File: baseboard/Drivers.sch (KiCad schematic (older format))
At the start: 9 parts, among them J6 Conn_01x08_Male, J7 Conn_01x08_Male, J8 CONN_01x06, J9 CONN_01x06

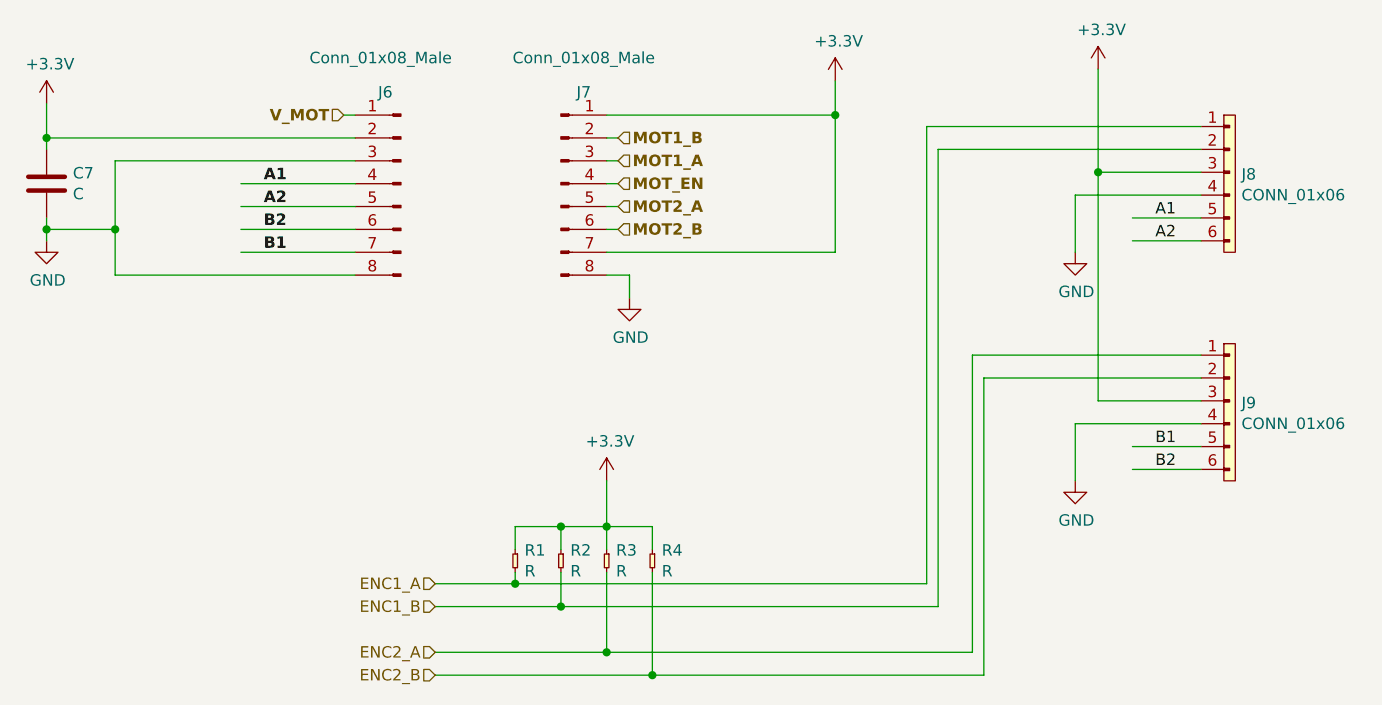
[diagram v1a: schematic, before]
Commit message: standalone version of unav2 based on stm32f405rgt
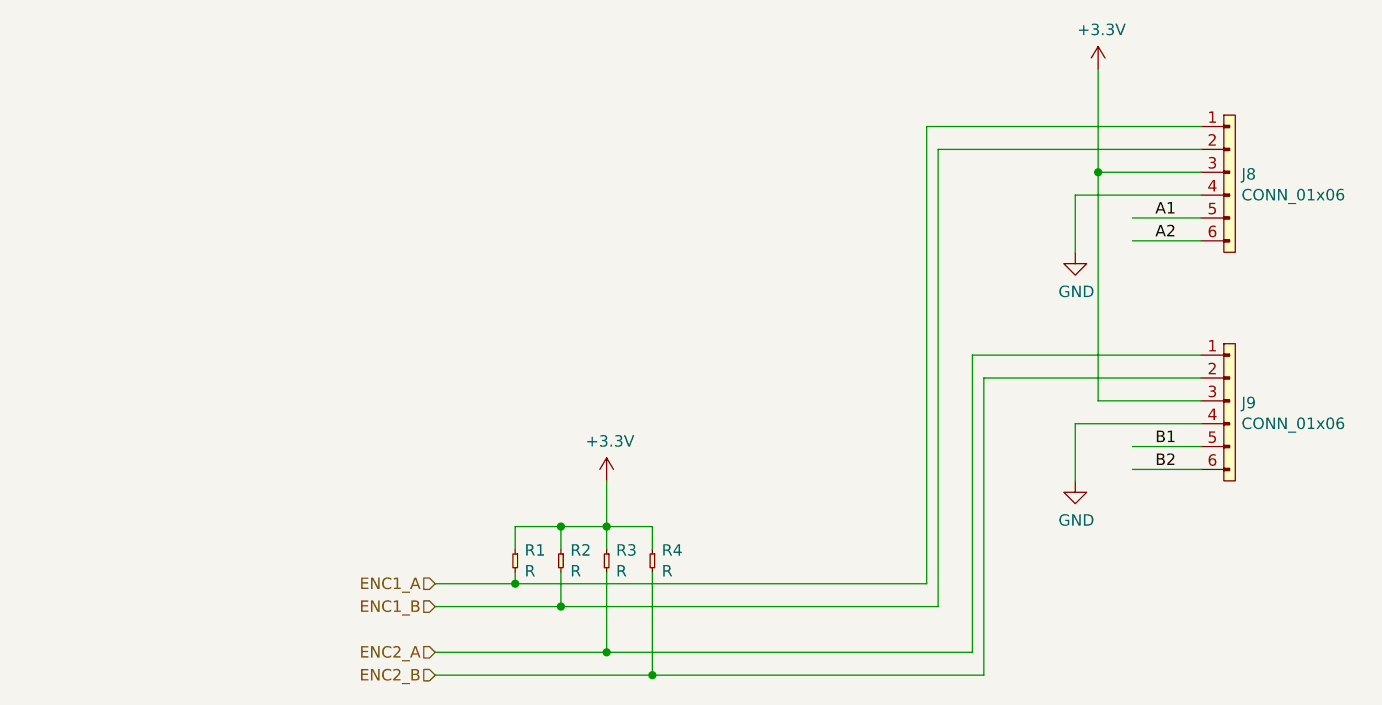
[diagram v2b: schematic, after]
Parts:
- removed C7: C, symbol Device:C
- removed J6, J7: Conn_01x08_Male, symbol Connector:Conn_01x08_Male
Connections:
- net labels removed: MOT1_A, MOT1_B, MOT2_A, MOT2_B, MOT_EN, V_MOT
- wire segments 66 -> 40
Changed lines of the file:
@@
 Comment4 ""
 $EndDescr
-$Comp
-L Connector:Conn_01x08_Male J7
-U 1 1 5B5238DA
-P 3400 2500
-F 0 "J7" H 3500 2900 50  0000 C CNN
-F 1 "Conn_01x08_Male" H 3500 3050 50  0000 C CNN
-F 2 "" H 3400 2500 50  0001 C CNN
-F 3 "~" H 3400 2500 50  0001 C CNN
-	1    3400 2500
-	1    0    0    -1
-$EndComp
-$Comp
-L Connector:Conn_01x08_Male J6
-U 1 1 5B523949
-P 2700 2500
-F 0 "J6" H 2800 2900 50  0000 R CNN
-F 1 "Conn_01x08_Male" H 3100 3050 50  0000 R CNN
-F 2 "" H 2700 2500 50  0001 C CNN
-F 3 "~" H 2700 2500 50  0001 C CNN
-	1    2700 2500
-	-1   0    0    -1
-$EndComp
-$Comp
-L power:+3.3V #PWR014
-U 1 1 5B524663
-P 1150 2150
-F 0 "#PWR014" H 1150 2000 50  0001 C CNN
-F 1 "+3.3V" H 1165 2323 50  0000 C CNN
-F 2 "" H 1150 2150 50  0001 C CNN
-F 3 "" H 1150 2150 50  0001 C CNN
-	1    1150 2150
-	1    0    0    -1
-$EndComp
-Wire Wire Line
-	1150 2300 2500 2300
-Wire Wire Line
-	1150 2150 1150 2300
-$Comp
-L Device:C C7
-U 1 1 5B5252BC
-P 1150 2500
-F 0 "C7" H 1265 2546 50  0000 L CNN
-F 1 "C" H 1265 2455 50  0000 L CNN
-F 2 "" H 1188 2350 50  0001 C CNN
-F 3 "~" H 1150 2500 50  0001 C CNN
-	1    1150 2500
-	1    0    0    -1
-$EndComp
-Wire Wire Line
-	1150 2350 1150 2300
-Connection ~ 1150 2300
-$Comp
-L power:GND #PWR015
-U 1 1 5B5254DA
-P 1150 2750
-F 0 "#PWR015" H 1150 2500 50  0001 C CNN
-F 1 "GND" H 1155 2577 50  0000 C CNN
-F 2 "" H 1150 2750 50  0001 C CNN
-F 3 "" H 1150 2750 50  0001 C CNN
-	1    1150 2750
-	1    0    0    -1
-$EndComp
-Wire Wire Line
-	1150 2750 1150 2700
-Wire Wire Line
-	1150 2700 1450 2700
-Wire Wire Line
-	1450 2700 1450 2400
-Wire Wire Line
-	1450 2400 2500 2400
-Connection ~ 1150 2700
-Wire Wire Line
-	1150 2700 1150 2650
-Wire Wire Line
-	2000 2500 2500 2500
-Wire Wire Line
-	2000 2600 2500 2600
-Wire Wire Line
-	2000 2700 2500 2700
-Wire Wire Line
-	2000 2800 2500 2800
-Wire Wire Line
-	1450 2700 1450 2900
-Wire Wire Line
-	1450 2900 2500 2900
-Connection ~ 1450 2700
-Text Label 2100 2500 0    50   ~ 10
-A1
-Text Label 2100 2600 0    50   ~ 10
-A2
-Text Label 2100 2700 0    50   ~ 10
-B2
-Text Label 2100 2800 0    50   ~ 10
-B1
-$Comp
-L power:+3.3V #PWR018
-U 1 1 5B527271
-P 4600 2050
-F 0 "#PWR018" H 4600 1900 50  0001 C CNN
-F 1 "+3.3V" H 4615 2223 50  0000 C CNN
-F 2 "" H 4600 2050 50  0001 C CNN
-F 3 "" H 4600 2050 50  0001 C CNN
-	1    4600 2050
-	1    0    0    -1
-$EndComp
-Wire Wire Line
-	4600 2200 4600 2050
-Wire Wire Line
-	3600 2200 4600 2200
-Wire Wire Line
-	4600 2800 4600 2200
-Wire Wire Line
-	3600 2800 4600 2800
-Connection ~ 4600 2200
-$Comp
-L power:GND #PWR017
-U 1 1 5B527C88
-P 3700 3000
-F 0 "#PWR017" H 3700 2750 50  0001 C CNN
-F 1 "GND" H 3705 2827 50  0000 C CNN
-F 2 "" H 3700 3000 50  0001 C CNN
-F 3 "" H 3700 3000 50  0001 C CNN
-	1    3700 3000
-	1    0    0    -1
-$EndComp
-Wire Wire Line
-	3600 2900 3700 2900
-Wire Wire Line
-	3700 2900 3700 3000
-Text HLabel 3650 2400 2    50   Input ~ 10
-MOT1_A
-Text HLabel 3650 2300 2    50   Input ~ 10
-MOT1_B
-Wire Wire Line
-	3650 2300 3600 2300
-Wire Wire Line
-	3600 2400 3650 2400
-Text HLabel 3650 2500 2    50   Input ~ 10
-MOT_EN
-Text HLabel 3650 2600 2    50   Input ~ 10
-MOT2_A
-Text HLabel 3650 2700 2    50   Input ~ 10
-MOT2_B
-Wire Wire Line
-	3600 2500 3650 2500
-Wire Wire Line
-	3650 2600 3600 2600
-Wire Wire Line
-	3600 2700 3650 2700
-Text HLabel 2450 2200 0    50   Input ~ 10
-V_MOT
-Wire Wire Line
-	2450 2200 2500 2200
 Text HLabel 2850 4250 0    50   Input ~ 0
 ENC1_A
